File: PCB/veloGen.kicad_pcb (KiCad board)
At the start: 2 copper layers, 47 parts, among them J1 CONN_01X02, J2 Gen. IN, J3 Batt, P1 TTL_232R_3V3, P2 CONN_01X04, Q1 STL4P3LLH6, Q2 BSS138_ok, Q3 STL6N3LLH6, U1 ESP-WROOM-32, U2 TS1101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

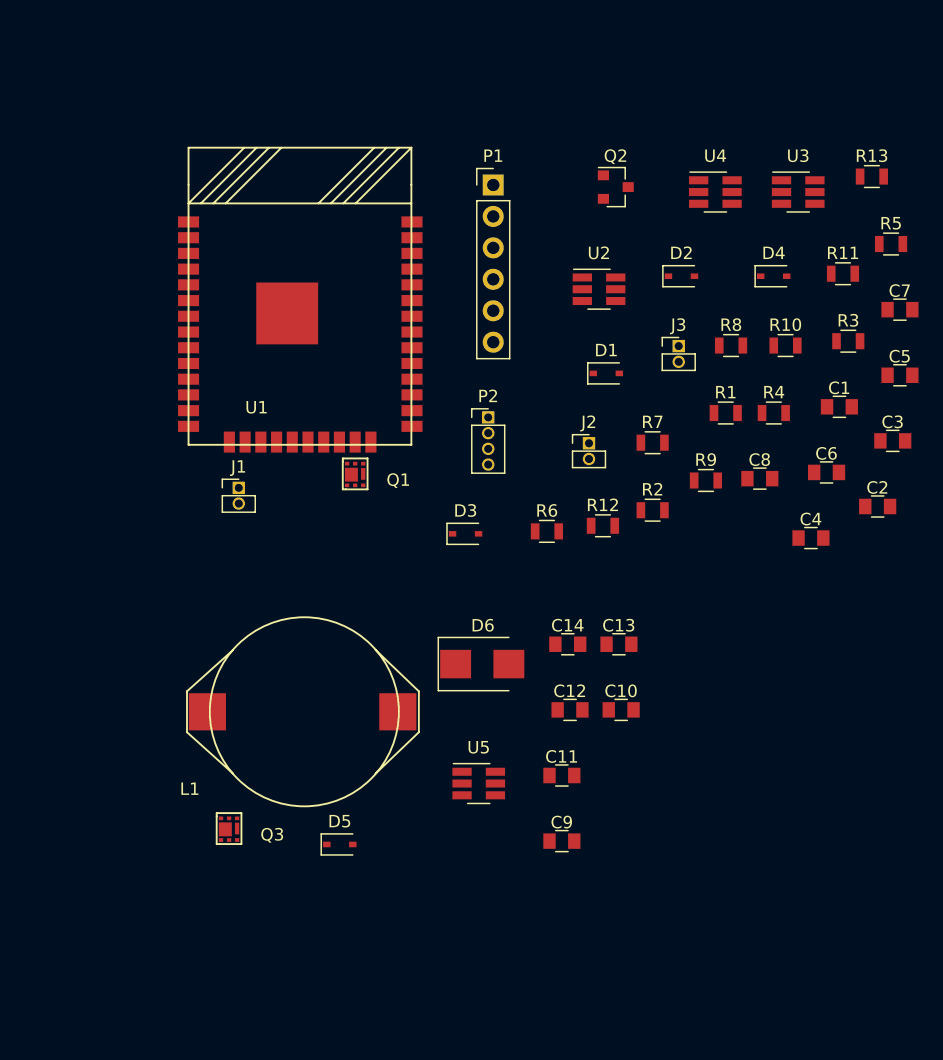
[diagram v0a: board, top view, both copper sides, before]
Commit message: Moved around some components a bit
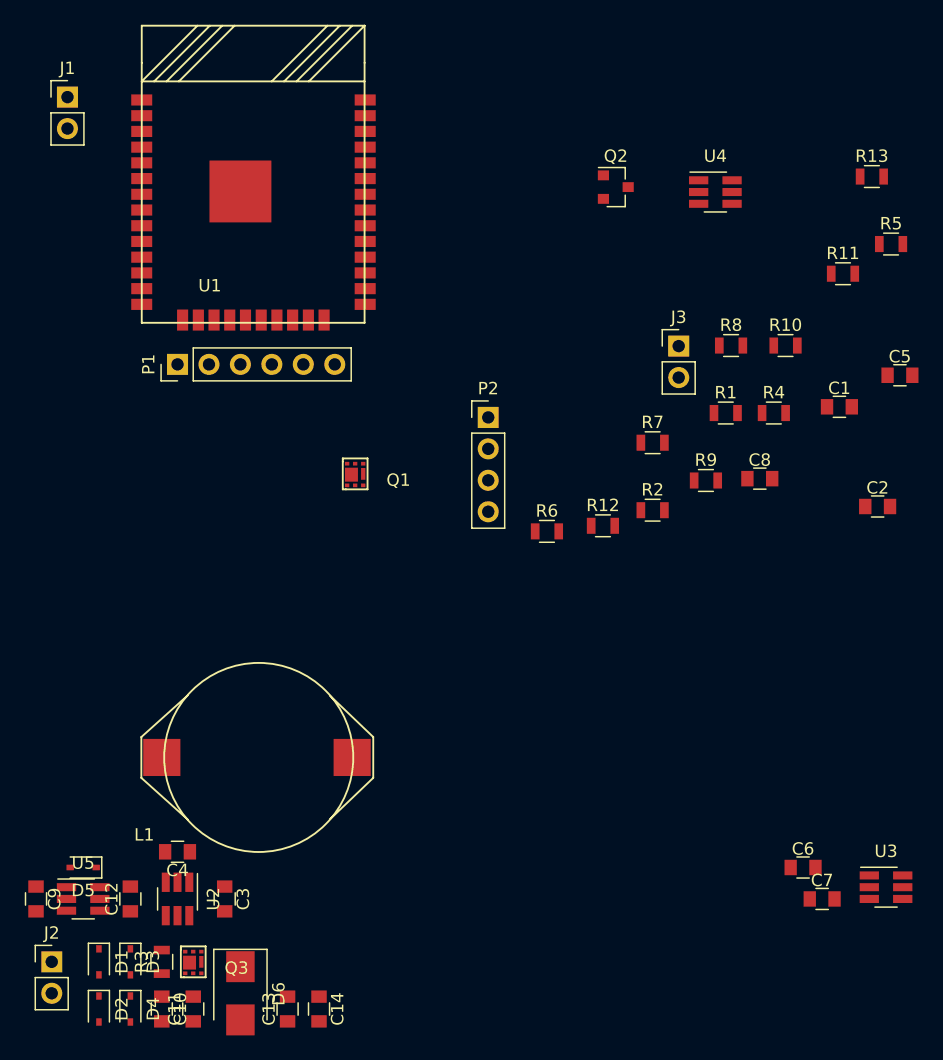
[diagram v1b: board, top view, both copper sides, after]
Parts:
- J1, J2, J3: footprint Pin_Headers:Pin_Header_Straight_1x02_Pitch1.27mm -> Pin_Headers:Pin_Header_Straight_1x02_Pitch2.54mm
- P2: footprint Pin_Headers:Pin_Header_Straight_1x04_Pitch1.27mm -> Pin_Headers:Pin_Header_Straight_1x04_Pitch2.54mm
- R3, R8: value R005 -> R050
- moved D4 78.8 mm to (35.6, 102.9), turned to 270 degrees
- moved D2 75.6 mm to (33.0, 102.9), turned to 270 degrees
- moved R3 74.8 mm to (38.1, 99.1), turned to 90 degrees
- moved C3 65.4 mm to (43.2, 94.0), turned to 270 degrees
- moved D1 62.8 mm to (33.0, 99.1), turned to 270 degrees
- moved J2 60.3 mm to (29.2, 99.1)
- moved U2 59.9 mm to (39.4, 94.0), turned to 270 degrees
- moved C4 57.1 mm to (39.4, 90.2), turned to 180 degrees
- moved U3 56.6 mm to (96.6, 93.0)
- moved C7 48.0 mm to (91.4, 94.0)
- moved C10 44.3 mm to (38.1, 102.9), turned to 270 degrees
- moved D3 43.9 mm to (35.6, 99.1), turned to 270 degrees
- moved C9 42.7 mm to (27.9, 94.0), turned to 270 degrees
- moved C13 39.8 mm to (48.3, 102.9), turned to 90 degrees
- moved C12 38.7 mm to (35.6, 94.0), turned to 90 degrees
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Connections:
- J3 pad 1: (no net) -> Net-(J3-Pad1)
- P1 pad 2: (no net) -> Net-(P1-Pad2)
- P1 pad 3: (no net) -> Net-(P1-Pad3)
- R3 pad 1: Net-(D1-Pad1) -> /BuckConv./vIn
- R3 pad 2: Net-(R3-Pad2) -> Net-(D1-Pad1)
- R8 pad 1: +BATT -> Net-(J3-Pad1)
- R8 pad 2: Net-(R8-Pad2) -> +BATT
- U1 pad 10: (no net) -> Net-(U1-Pad10)
- U1 pad 11: (no net) -> Net-(U1-Pad11)
- U1 pad 12: (no net) -> Net-(U1-Pad12)
- U1 pad 13: (no net) -> Net-(U1-Pad13)
- U1 pad 14: (no net) -> Net-(U1-Pad14)
- U1 pad 16: (no net) -> Net-(U1-Pad16)
- U1 pad 17: (no net) -> Net-(U1-Pad17)
- U1 pad 18: (no net) -> Net-(U1-Pad18)
- U1 pad 19: (no net) -> Net-(U1-Pad19)
- U1 pad 20: (no net) -> Net-(U1-Pad20)
- U1 pad 21: (no net) -> Net-(U1-Pad21)
- U1 pad 22: (no net) -> Net-(U1-Pad22)
- U1 pad 23: (no net) -> Net-(U1-Pad23)
- U1 pad 24: (no net) -> Net-(U1-Pad24)
- U1 pad 32: (no net) -> Net-(U1-Pad32)
- U1 pad 33: (no net) -> Net-(U1-Pad33)
- U1 pad 36: (no net) -> Net-(U1-Pad36)
- U1 pad 37: (no net) -> Net-(U1-Pad37)
- U1 pad 8: (no net) -> Net-(U1-Pad8)
- U1 pad 9: (no net) -> Net-(U1-Pad9)
- U2 pad 2: (no net) -> Net-(U2-Pad2)
- U2 pad 4: (no net) -> /BuckConv./vIn
- U2 pad 6: Net-(R3-Pad2) -> Net-(D1-Pad1)
- U3 pad 4: (no net) -> Net-(J3-Pad1)
- U3 pad 6: Net-(R8-Pad2) -> +BATT
- U4 pad 6: (no net) -> Net-(U4-Pad6)

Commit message: Layout ideas
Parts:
- added R14: 470, Resistors_SMD:R_0805, F.Cu at (39.4, 91.2)
- C1, C2, C3, C4, C5, C6, C7, Q1, Q2, R10, R11, R12, R13, R2, R3, R4, R5, R6, R7, R9, U2, U3: moved to B.Cu
- L1: value L -> 68u; footprint myStuff:cc_5022 -> myStuff:MSS1048; moved to B.Cu
- moved C8 75.0 mm to (11.4, 62.2), turned to 270 degrees
- moved R1 72.8 mm to (23.4, 95.5)
- moved U4 72.2 mm to (15.2, 62.2)
- moved U3 68.1 mm to (28.7, 88.4), turned to 270 degrees
- moved R5 65.1 mm to (42.2, 76.2), turned to 90 degrees
- moved C7 63.4 mm to (28.7, 84.8)
- moved C6 61.5 mm to (28.4, 91.9)
- moved C1 60.0 mm to (33.0, 58.4), turned to 90 degrees
- moved R13 58.6 mm to (44.9, 65.2), turned to 90 degrees
- moved C2 58.0 mm to (39.6, 76.2), turned to 90 degrees
- moved C5 58.0 mm to (42.3, 68.7), turned to 90 degrees
- moved P1 54.7 mm to (-15.2, 48.3), turned to 180 degrees
- moved J3 51.4 mm to (31.8, 67.3), turned to 270 degrees
- moved R11 50.3 mm to (46.1, 61.4)
- moved R4 48.7 mm to (42.2, 72.4), turned to 90 degrees
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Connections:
- U5 pad 5: Net-(Q3-Pad1) -> Net-(R14-Pad2)
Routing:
- net /BuckConv./vIn: track 0.00 -> 18.5 mm, vias 0 -> 1
- net Net-(C12-Pad1): track 0.00 -> 12.5 mm, vias 0 -> 2
- net Net-(D1-Pad1): track 0.00 -> 10.3 mm, vias 0 -> 1
- net Net-(D3-Pad2): track 0.00 -> 7.88 mm
- net Net-(C10-Pad2): track 0.00 -> 6.40 mm
- net Net-(R14-Pad2): track 0.00 -> 5.00 mm
- net +3V3: track 0.00 -> 4.77 mm, vias 0 -> 1
- net Net-(D1-Pad2): track 0.00 -> 4.77 mm
- net GND: track 0.00 -> 4.77 mm
- net Net-(C12-Pad2): track 0.00 -> 4.49 mm
- net /IbattSign: track 0.00 -> 3.98 mm
- net +BATT: track 0.00 -> 3.19 mm
- net Net-(Q3-Pad1): track 0.00 -> 2.98 mm
- net /Igen: track 0.00 -> 2.23 mm
- net /Ibatt: track 0.00 -> 2.22 mm

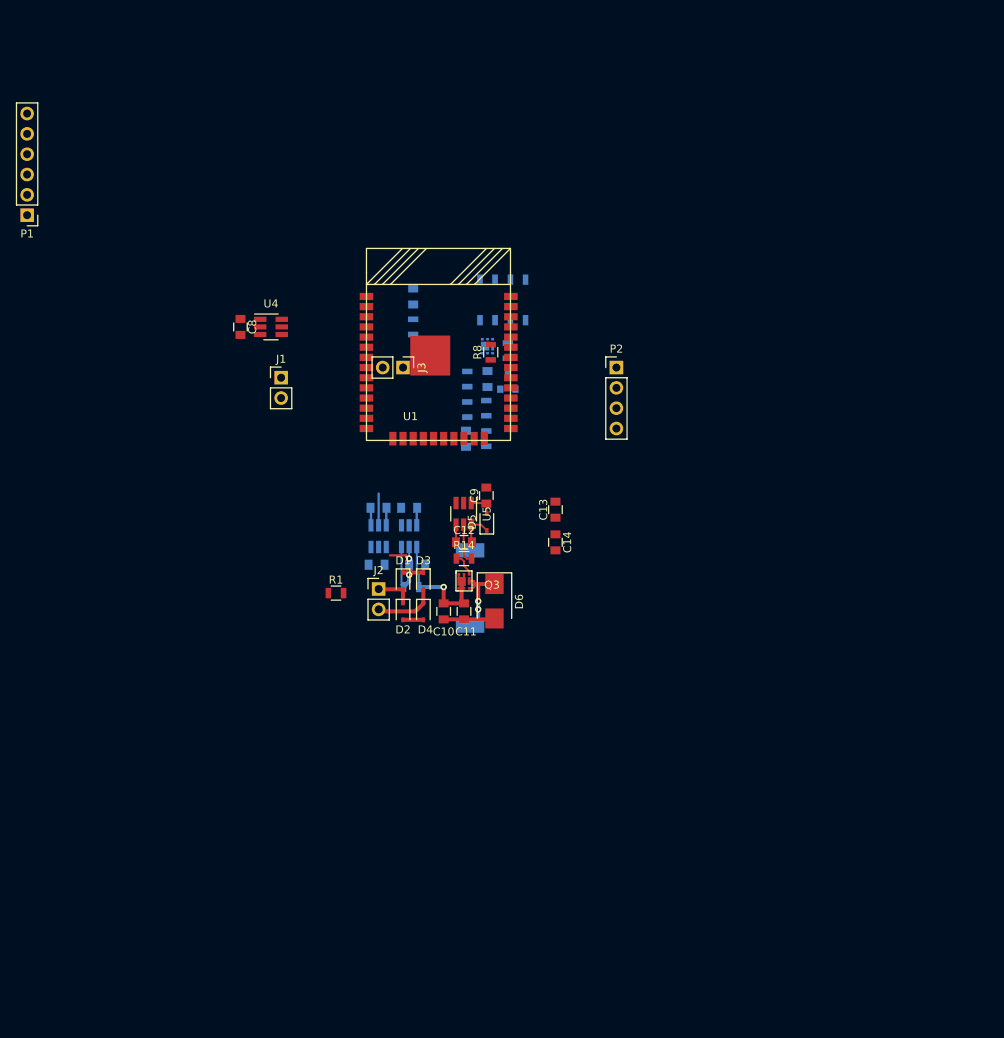
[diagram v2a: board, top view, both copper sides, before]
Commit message: Simplified schematic and started layout
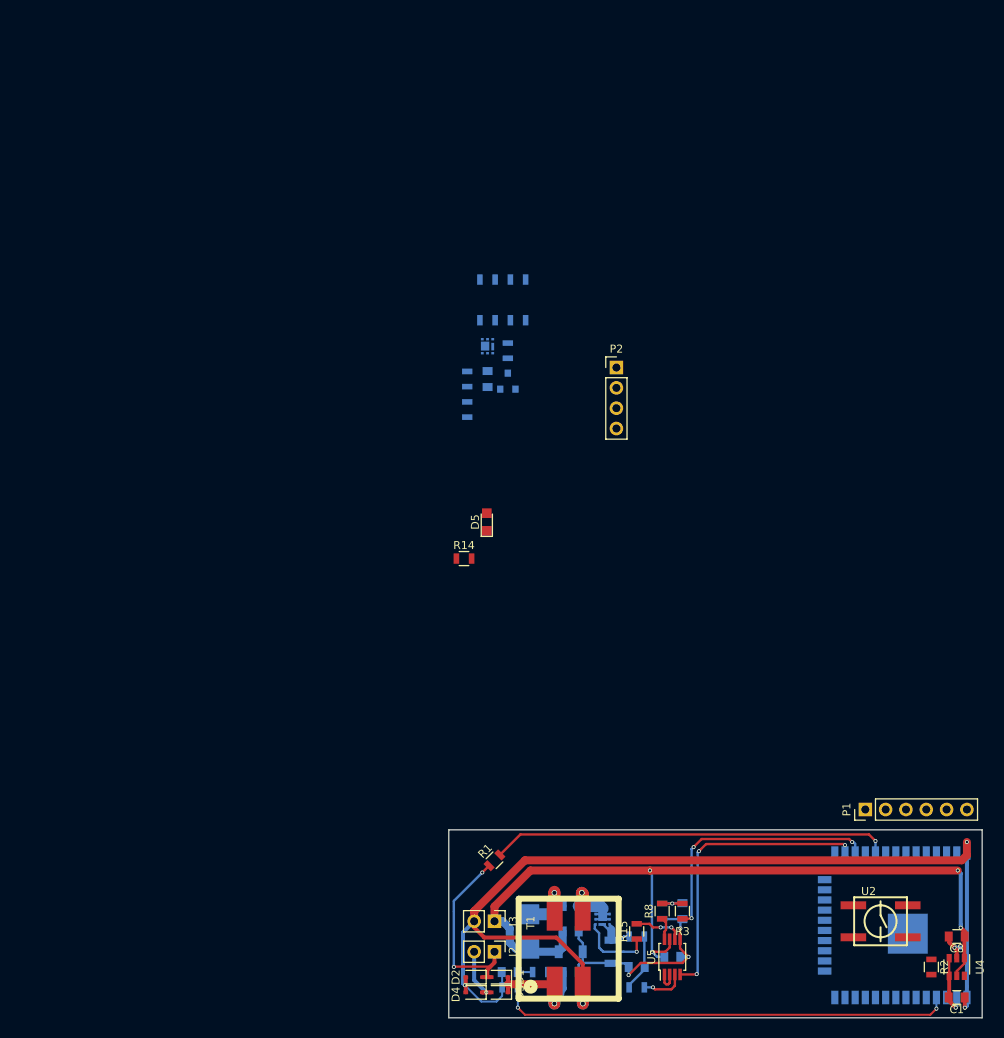
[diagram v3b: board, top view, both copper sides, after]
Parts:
- removed C12, C9: 470n, Capacitors_SMD:C_0805
- removed C7: 47n, Capacitors_SMD:C_0805
- removed J1: CONN_01X02, Pin_Headers:Pin_Header_Straight_1x02_Pitch2.54mm
- removed L1: 68u, myStuff:MSS1048
- removed U3: TS1101, TO_SOT_Packages_SMD:SOT-23-6_Handsoldering
- added C15: 470n, Capacitors_SMD:C_0805, B.Cu at (52.7, 137.8)
- added R15: 10R, Resistors_SMD:R_0805, F.Cu at (61.0, 137.8)
- added R16: 0.1R, Resistors_SMD:R_1206, B.Cu at (57.8, 140.3)
- added R17: 1k15, Resistors_SMD:R_0805, B.Cu at (64.1, 135.3)
- added R18: 4k7, Resistors_SMD:R_0805, B.Cu at (61.0, 144.8)
- added R19: 4k7, Resistors_SMD:R_0805, B.Cu at (61.0, 138.4)
- added T1: MSD1260, myStuff:MSD1260, F.Cu at (52.7, 139.7)
- C1, R2: moved to F.Cu
- C10, C14: value 10u -> 22u; footprint Capacitors_SMD:C_0805 -> Capacitors_SMD:C_1206; moved to B.Cu
- C11, D6, Q3, U1: moved to B.Cu
- C13: value 470n -> 1u; moved to B.Cu
- C3: value 470n -> 47n
- C4: value 47n -> 47p
- D5: value B5819WS -> LED; footprint Diodes_SMD:D_SOD-323 -> LEDs:LED_0805
- J3: value Batt -> Bat
- R14: value 470 -> 470R
- R3: value R050 -> 4k7; moved to F.Cu
- R8: value R050 -> 4k7
- U2: value TS1101 -> PROG; footprint TO_SOT_Packages_SMD:SOT-23-6_Handsoldering -> myStuff:EVQQ2; moved to F.Cu
- U4: footprint TO_SOT_Packages_SMD:SOT-23-6_Handsoldering -> TO_SOT_Packages_SMD:SOT-23-6
- U5: value LTC4440-5 -> MCP1630; footprint TO_SOT_Packages_SMD:SOT-23-6_Handsoldering -> Housings_SSOP:MSOP-8_3x3mm_Pitch0.65mm
- moved P1 128.4 mm to (89.5, 122.6), turned to 90 degrees
- moved C8 117.6 mm to (101.0, 138.4), turned to 180 degrees
- moved U4 117.3 mm to (101.0, 142.2), turned to 270 degrees
- moved U1 115.4 mm to (102.2, 146.1), turned to 90 degrees
- moved C1 110.9 mm to (101.0, 146.1), turned to 180 degrees
- moved R2 102.9 mm to (97.8, 142.2), turned to 270 degrees
- moved U2 76.1 mm to (91.4, 136.5), turned to 0 degrees
- moved R8 73.1 mm to (64.1, 135.3)
- moved R4 70.8 mm to (48.9, 142.9), turned to 180 degrees
- moved J3 70.2 mm to (43.2, 136.5)
- moved R5 68.6 mm to (45.1, 144.8), turned to 180 degrees
- moved C2 66.9 mm to (45.1, 142.9), turned to 180 degrees
- moved C4 64.1 mm to (61.0, 142.2), turned to 180 degrees
- moved C6 61.4 mm to (65.4, 141.0), turned to 180 degrees
- moved U5 61.2 mm to (65.4, 141.0), turned to 90 degrees
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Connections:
- C10 pad 1: /BuckConv./vIn -> /SepicConv./vIn
- C10 pad 2: Net-(C10-Pad2) -> GND
- C11 pad 1: Net-(C10-Pad2) -> GND
- C11 pad 2: /BuckConv./vIn -> /SepicConv./vIn
- C13 pad 1: Net-(C10-Pad2) -> Net-(C13-Pad1)
- C13 pad 2: +BATT -> Net-(C13-Pad2)
- C14 pad 2: Net-(C10-Pad2) -> GND
- C3 pad 1: GND -> Net-(C3-Pad1)
- C3 pad 2: +3V3 -> GND
- C4 pad 1: GND -> Net-(C4-Pad1)
- C4 pad 2: /Igen -> GND
- C6 pad 2: +3V3 -> +BATT
- D1 pad 1: Net-(D1-Pad1) -> /SepicConv./vIn
- D3 pad 1: Net-(D1-Pad1) -> /SepicConv./vIn
- D5 pad 1: Net-(C12-Pad2) -> GND
- D5 pad 2: +BATT -> Net-(D5-Pad2)
- D6 pad 1: Net-(C12-Pad1) -> +BATT
- D6 pad 2: Net-(C10-Pad2) -> Net-(C13-Pad1)
- J3 pad 1: Net-(J3-Pad1) -> +BATT
- P1 pad 6: Net-(P1-Pad6) -> /rstBtn
- Q3 pad 2: Net-(C12-Pad1) -> Net-(Q3-Pad2)
- Q3 pad 3: /BuckConv./vIn -> Net-(C13-Pad2)
- R14 pad 1: Net-(Q3-Pad1) -> Net-(R14-Pad1)
- R14 pad 2: Net-(R14-Pad2) -> Net-(D5-Pad2)
- R3 pad 1: /BuckConv./vIn -> Net-(C3-Pad1)
- R3 pad 2: Net-(D1-Pad1) -> /sepicImax
- R4 pad 1: /BuckConv./vIn -> /SepicConv./vIn
- R8 pad 1: Net-(J3-Pad1) -> Net-(R8-Pad1)
- R8 pad 2: +BATT -> Net-(C3-Pad1)
- U1 pad 14: Net-(U1-Pad14) -> Net-(R14-Pad1)
- U1 pad 25: Net-(P1-Pad6) -> Net-(U1-Pad25)
- U1 pad 26: /buckPwm -> /sepicPwm
- U1 pad 27: /vExtEnable -> /sepicImax
- U1 pad 28: /IbattSign -> /vExtEnable
- U1 pad 6: /Ibatt -> Net-(U1-Pad6)
- U1 pad 7: /Igen -> Net-(U1-Pad7)
- U5 pad 1: +BATT -> Net-(U5-Pad1)
- U5 pad 2: GND -> Net-(U5-Pad1)
- U5 pad 3: /buckPwm -> Net-(R18-Pad2)
- U5 pad 4: Net-(C12-Pad1) -> /sepicPwm
- U5 pad 5: Net-(R14-Pad2) -> GND
- U5 pad 6: Net-(C12-Pad2) -> Net-(R15-Pad2)
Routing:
- net GND: track 4.77 -> 169.4 mm, vias 0 -> 8
- net +BATT: track 3.19 -> 104.5 mm, vias 0 -> 4
- net /Vgen: track 0.00 -> 60.8 mm, vias 0 -> 2
- net /speedPulse: track 0.00 -> 49.9 mm, vias 0 -> 1
- net /sepicPwm: track 0.00 -> 37.3 mm, vias 0 -> 3
- net /sepicImax: track 0.00 -> 32.4 mm, vias 0 -> 3
- net Net-(D1-Pad2): track 4.77 -> 24.8 mm, vias 0 -> 2
- net /SepicConv./vIn: track 0.00 -> 18.6 mm, vias 0 -> 1
- net /BuckConv./vIn: track 18.5 -> 0.00 mm, vias 1 -> 0
- net Net-(C13-Pad2): track 0.00 -> 13.4 mm, vias 0 -> 1
- net Net-(C12-Pad1): track 12.5 -> 0.00 mm, vias 2 -> 0
- net Net-(D1-Pad1): track 10.3 -> 0.00 mm, vias 1 -> 0
- net Net-(C13-Pad1): track 0.00 -> 9.58 mm, vias 0 -> 1
- net Net-(C4-Pad1): track 0.00 -> 7.18 mm
- net Net-(Q3-Pad1): track 2.98 -> 9.63 mm, vias 0 -> 1
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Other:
- board outline added: 66.7 x 23.5 mm
- net class Default: clearance 0.2 -> 0.27; trace_width 0.25 -> 0.3; via_dia 0.8 -> 0.5; via_drill 0.4 -> 0.3
- rule trace_clearance: 0.2 -> 0.27
- rule trace_min: 0.2 -> 0.3
- rule via_min_size: 0.4 -> 0.5

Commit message: completed an ugly pcb with minimalistic fuctionality
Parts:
- removed P1: TTL_232R_3V3, Pin_Headers:Pin_Header_Straight_1x06_Pitch2.54mm
- removed P2: CONN_01X04, Pin_Headers:Pin_Header_Straight_1x04_Pitch2.54mm
- removed Q1: STL4P3LLH6, myStuff:PowerFLAT_2x2
- removed Q2: BSS138_ok, TO_SOT_Packages_SMD:SOT-23
- removed R10, R9: 200R, Resistors_SMD:R_0805
- removed R11, R12: 4k7, Resistors_SMD:R_0805
- removed R13: 4.7Meg, Resistors_SMD:R_0805
- removed U2: PROG, myStuff:EVQQ2
- added J1: Conn_01x06, myStuff:myPogoPads, B.Cu at (78.7, 128.3)
- C5, R6, R7: moved to F.Cu
- D5, R14: moved to B.Cu
- moved R7 73.6 mm to (76.2, 132.7), turned to 0 degrees
- moved R6 72.4 mm to (80.0, 132.7), turned to 180 degrees
- moved C5 70.7 mm to (72.4, 132.7), turned to 180 degrees
- moved R14 67.6 mm to (80.6, 144.8), turned to 90 degrees
- moved D5 66.0 mm to (80.6, 140.3), turned to 270 degrees
- moved R2 2.54 mm to (97.8, 144.8)
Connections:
- U1 pad 25: Net-(U1-Pad25) -> /progFlag
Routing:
- net /Vbatt: track 0.00 -> 42.8 mm, vias 0 -> 3
- net /rstBtn: track 0.00 -> 40.0 mm, vias 0 -> 1
- net GND: track 169.4 -> 199.5 mm, vias 8 -> 12
- net Net-(J1-Pad2): track 0.00 -> 24.3 mm
- net Net-(J1-Pad3): track 0.00 -> 19.3 mm
- net /progFlag: track 0.00 -> 8.72 mm
- net Net-(R14-Pad1): track 0.00 -> 5.21 mm
- net +BATT: track 104.5 -> 107.9 mm, vias 4 -> 3
- net Net-(D5-Pad2): track 0.00 -> 2.40 mm
- net +3V3: track 7.61 -> 9.87 mm
- net /sepicPwm: track 37.3 -> 38.0 mm
- added copper zone on B.Cu, net GND
- added copper zone on F.Cu, net GND
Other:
- board size 66.7 x 23.5 mm -> 67 x 24 mm
